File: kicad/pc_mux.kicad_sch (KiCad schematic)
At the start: 12 parts, among them U10 ATF22V10C-7PX, U3 ATF22V10C-10PU, U4 ATF22V10C-10PU, U7 ATF22V10C-7PX, U8 ATF22V10C-7PX, U9 ATF22V10C-7PX

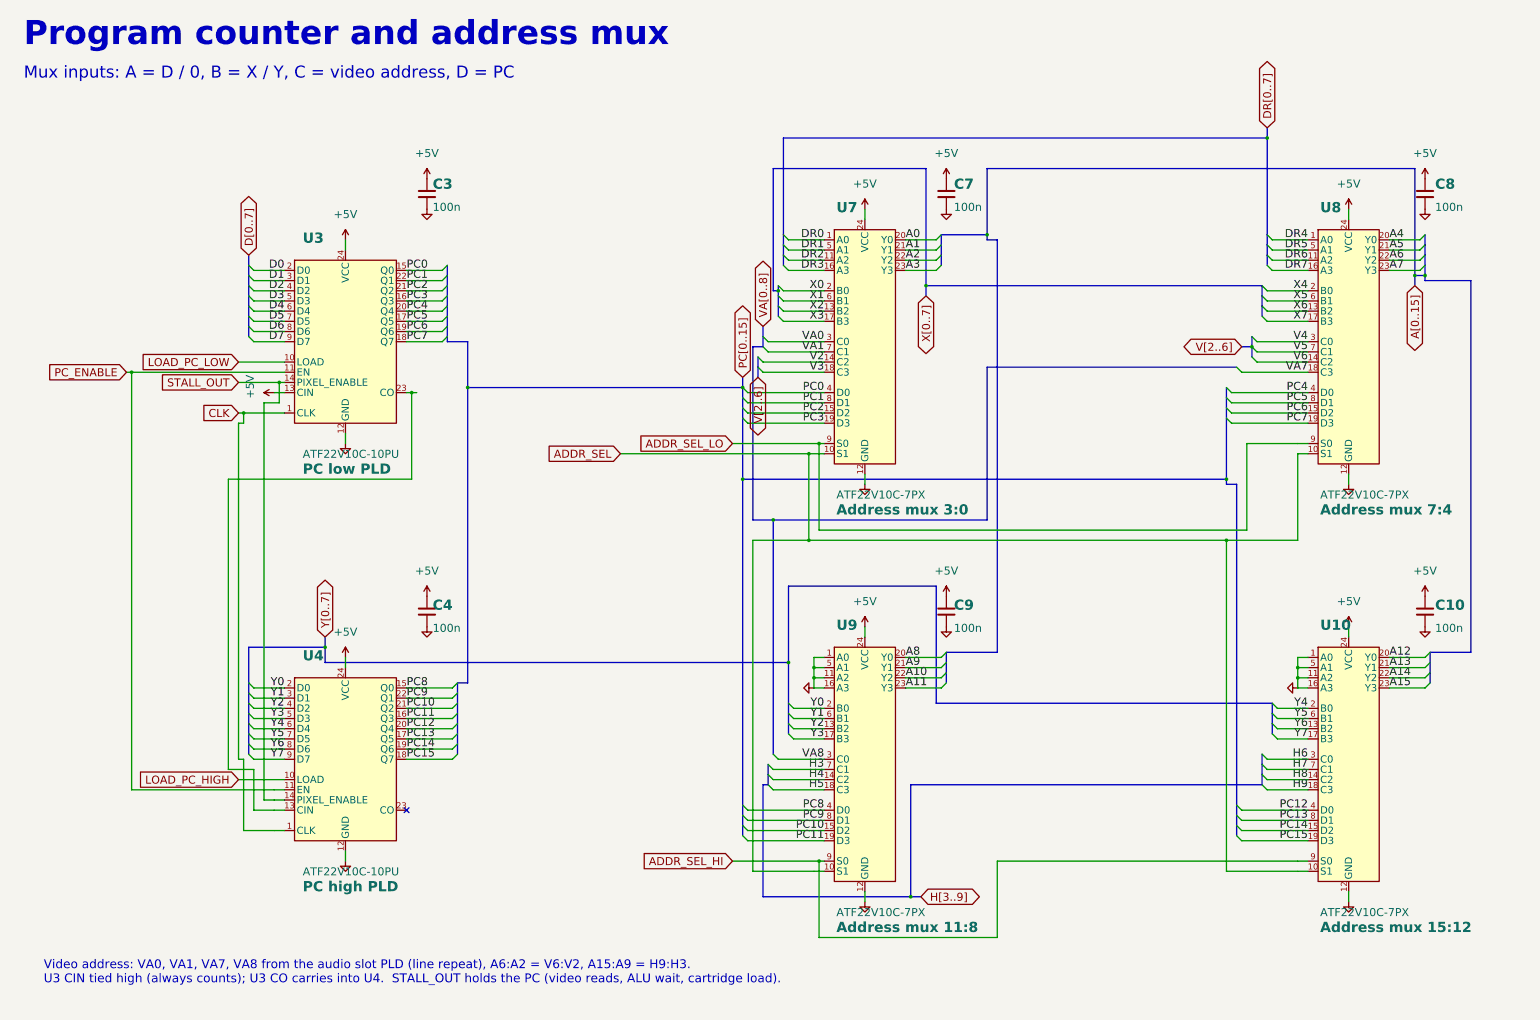
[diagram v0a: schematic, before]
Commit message: Tidy every schematic sheet: spread parts, straight runs, buses kept, horizontal tabs
Shared port, expansion and cartridge sheets laid out by hand; buses from
other sheets get a bus label at each chip, busy control nets a label at
each pin; some PLD and connector symbols reordered so wires run straight;
sideways power symbols read across. 0 netlist problems, no overlaps.

Co-Authored-By: Claude Opus 5.5 (1M context) <noreply@anthropic.com>
Claude-Session: https://claude.ai/code/session_01L9AkLuEg13EebxDmgXsaEp
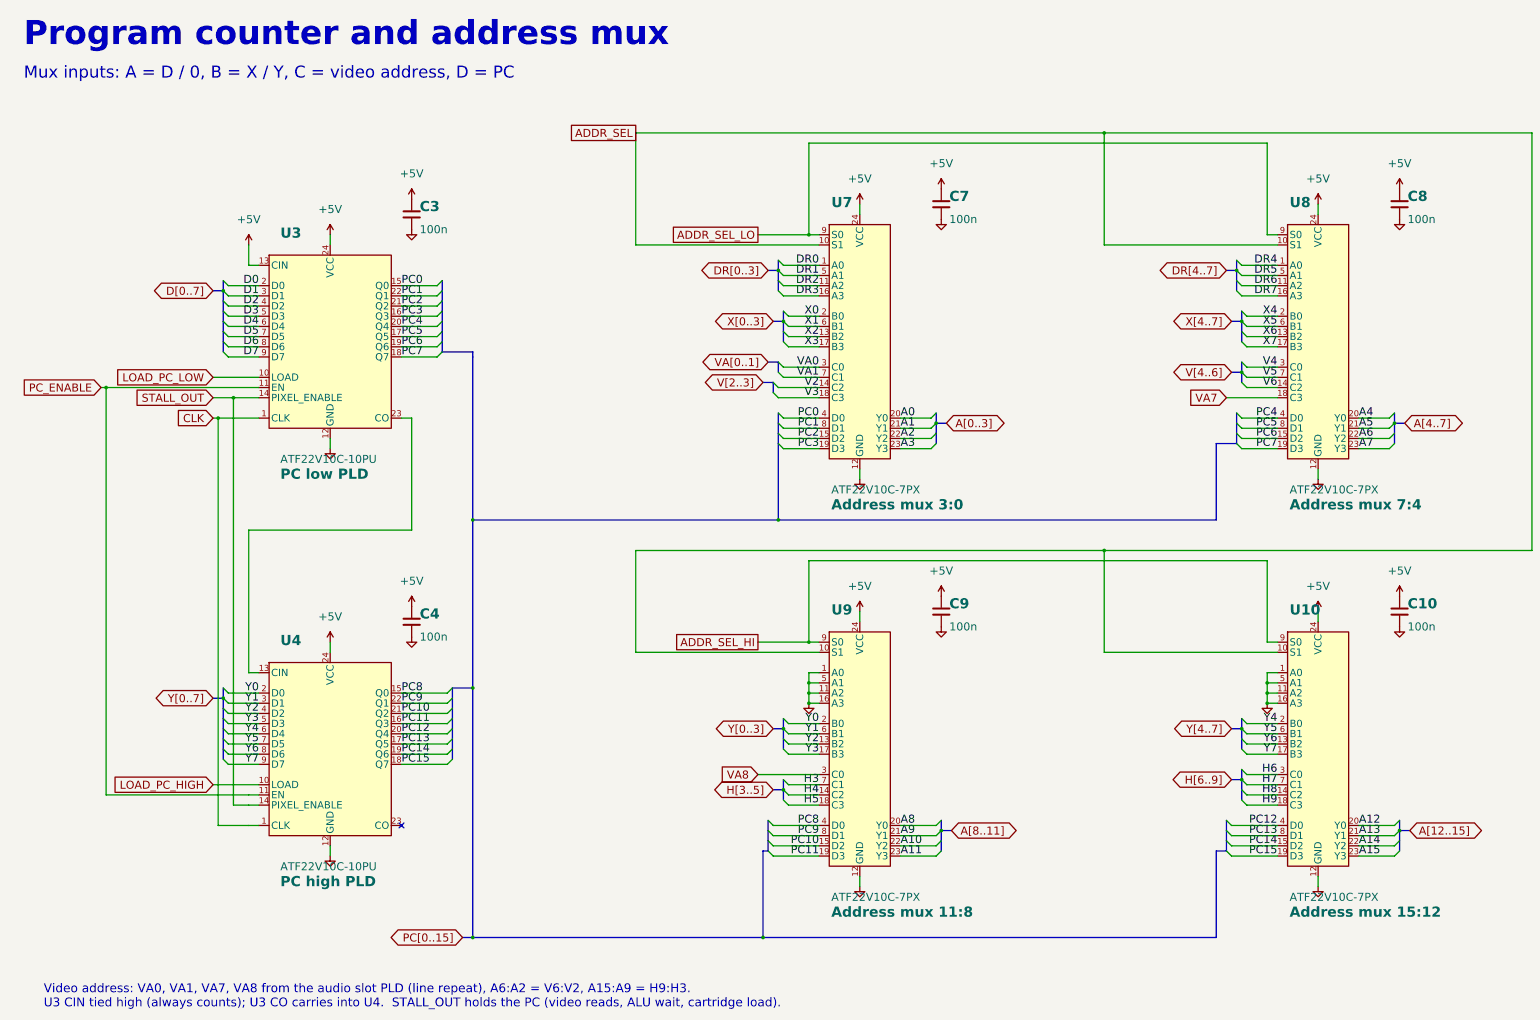
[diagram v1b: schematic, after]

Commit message: Bill of materials for the main board, cartridge and keyboard
Manufacturer and MPN fields on every schematic part (empty where none is
chosen), set from an MPN table in gen_kicad_schematic.py; net tie, cartridge
edge fingers and solder jumper excluded from the BOM.  gen_bom.py groups the
parts by part number into docs/BOM.md and docs/BOM.csv, adding sockets,
shunts, keyboard LEDs, keycaps, stabilizers and the keyboard ribbon cable.

Co-Authored-By: Claude Opus 5.5 (1M context) <noreply@anthropic.com>
Claude-Session: https://claude.ai/code/session_018iEnPngycbxX6Tt4Wzp3zN
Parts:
- U10, U7, U8, U9: MPN (none) -> ATF22V10C-7PX; Manufacturer (none) -> Microchip
- U3, U4: MPN (none) -> ATF22V10C-10PU; Manufacturer (none) -> Microchip

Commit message: Part numbers for the remaining parts; J6 Tensility 54-00174; optional J1 and J9-J12
Every schematic part gets Manufacturer/MPN: Yageo MFR-25 resistors by value,
Bourns 4609X networks, KEMET/TDK ceramics, Panasonic FR electrolytics, ECS
oscillator, Assmann VGA, Sullins headers, Wurth box header, Cherry switches.
Sockets get On Shore numbers (0.3" 24/28-pin are ED241DT/ED281DT; ED28DT is
0.6"). J6 becomes the Tensility 54-00174 TRRS jack with a footprint drawn
from its datasheet. Digi-Key prices from Justin for the oscillator, VGA and
audio jack. The expansion slot sockets and the keyboard header are optional,
with a BOM total without them.

Co-Authored-By: Claude Opus 5.5 (1M context) <noreply@anthropic.com>
Claude-Session: https://claude.ai/code/session_01L9AkLuEg13EebxDmgXsaEp
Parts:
- C10, C3, C4, C7, C8, C9: MPN (none) -> C320C104K5R5TA; Manufacturer (none) -> KEMET

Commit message: Every PLD is an ATF22V10C-7PX (one part number)
Justin: switch the seven main-board -10PU PLDs (Branch, PC x2, H, V,
color decoder, audio slot) and the cartridge loader to the -7PX, for one
part number to buy, program and kit (.52 more per main board). Symbols,
schematics, PDFs, BOM, docs and PLD comments updated; CHIPS.md keeps the
grade each PLD could use.

Co-Authored-By: Claude Opus 5.5 (1M context) <noreply@anthropic.com>
Claude-Session: https://claude.ai/code/session_01JnVuvUvdWezUUU6Sgmg16H
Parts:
- U3, U4: value ATF22V10C-10PU -> ATF22V10C-7PX; MPN ATF22V10C-10PU -> ATF22V10C-7PX
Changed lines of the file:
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@@
   (wire (pts (xy 91.44 119.38) (xy 91.44 121.92)) (stroke (width 0) (type default)))
   (symbol (lib_id "power:GND") (at 91.44 121.92 0) (unit 1) (in_bom yes) (on_board yes) (dnp no) (property "Reference" "#PWR0402" (at 91.44 121.92 0) (effects (font (size 1.27 1.27)) hide)) (property "Value" "GND" (at 91.44 128.27 0) (effects (font (size 2 2)) hide)) (property "Footprint" "" (at 91.44 121.92 0) (effects (font (size 1.27 1.27)) hide)) (property "Datasheet" "" (at 91.44 121.92 0) (effects (font (size 1.27 1.27)) hide)) (pin "1") (instances (project "placard" (path "/e3450542-4ffc-59d4-a4a7-45636233928a/cfc9d041-a0ad-5edc-9a97-521f7f69130f" (reference "#PWR0402") (unit 1)))))
-  (symbol (lib_id "placard:ATF22V10C_PC_COUNTER8") (at 91.44 93.98 0) (unit 1) (in_bom yes) (on_board yes) (dnp no) (property "Reference" "U3" (at 78.994 69.62 0) (effects (font (size 2.54 2.54) bold) (justify left bottom))) (property "Value" "ATF22V10C-10PU" (at 78.994 123.38 0) (effects (font (size 2 2)) (justify left top))) (property "Function" "PC low PLD" (at 78.994 126.78 0) (effects (font (size 2.54 2.54) bold) (justify left top))) (property "Footprint" "Package_DIP:DIP-24_W7.62mm" (at 91.44 93.98 0) (effects (font (size 1.27 1.27)) hide)) (property "Datasheet" "https://ww1.microchip.com/downloads/en/DeviceDoc/doc0735.pdf" (at 91.44 93.98 0) (effects (font (size 1.27 1.27)) hide)) (property "Manufacturer" "Microchip" (at 91.44 93.98 0) (effects (font (size 1.27 1.27)) hide)) (property "MPN" "ATF22V10C-10PU" (at 91.44 93.98 0) (effects (font (size 1.27 1.27)) hide)) (property "PLD" "ATF22V10_PC_COUNTER8.pld" (at 91.44 93.98 0) (effects (font (size 1.27 1.27)) hide)) (pin "13") (pin "2") (pin "3") (pin "4") (pin "5") (pin "6") (pin "7") (pin "8") (pin "9") (pin "10") (pin "11") (pin "14") (pin "1") (pin "15") (pin "22") (pin "21") (pin "16") (pin "20") (pin "17") (pin "19") (pin "18") (pin "23") (pin "24") (pin "12") (instances (project "placard" (path "/e3450542-4ffc-59d4-a4a7-45636233928a/cfc9d041-a0ad-5edc-9a97-521f7f69130f" (reference "U3") (unit 1)))))
+  (symbol (lib_id "placard:ATF22V10C_PC_COUNTER8") (at 91.44 93.98 0) (unit 1) (in_bom yes) (on_board yes) (dnp no) (property "Reference" "U3" (at 78.994 69.62 0) (effects (font (size 2.54 2.54) bold) (justify left bottom))) (property "Value" "ATF22V10C-7PX" (at 78.994 123.38 0) (effects (font (size 2 2)) (justify left top))) (property "Function" "PC low PLD" (at 78.994 126.78 0) (effects (font (size 2.54 2.54) bold) (justify left top))) (property "Footprint" "Package_DIP:DIP-24_W7.62mm" (at 91.44 93.98 0) (effects (font (size 1.27 1.27)) hide)) (property "Datasheet" "https://ww1.microchip.com/downloads/en/DeviceDoc/doc0735.pdf" (at 91.44 93.98 0) (effects (font (size 1.27 1.27)) hide)) (property "Manufacturer" "Microchip" (at 91.44 93.98 0) (effects (font (size 1.27 1.27)) hide)) (property "MPN" "ATF22V10C-7PX" (at 91.44 93.98 0) (effects (font (size 1.27 1.27)) hide)) (property "PLD" "ATF22V10_PC_COUNTER8.pld" (at 91.44 93.98 0) (effects (font (size 1.27 1.27)) hide)) (pin "13") (pin "2") (pin "3") (pin "4") (pin "5") (pin "6") (pin "7") (pin "8") (pin "9") (pin "10") (pin "11") (pin "14") (pin "1") (pin "15") (pin "22") (pin "21") (pin "16") (pin "20") (pin "17") (pin "19") (pin "18") (pin "23") (pin "24") (pin "12") (instances (project "placard" (path "/e3450542-4ffc-59d4-a4a7-45636233928a/cfc9d041-a0ad-5edc-9a97-521f7f69130f" (reference "U3") (unit 1)))))
   (symbol (lib_id "power:+5V") (at 111.76 59.69 0) (unit 1) (in_bom yes) (on_board yes) (dnp no) (property "Reference" "#PWR0403" (at 111.76 59.69 0) (effects (font (size 1.27 1.27)) hide)) (property "Value" "+5V" (at 111.76 53.34 0) (effects (font (size 2 2)))) (property "Footprint" "" (at 111.76 59.69 0) (effects (font (size 1.27 1.27)) hide)) (property "Datasheet" "" (at 111.76 59.69 0) (effects (font (size 1.27 1.27)) hide)) (pin "1") (instances (project "placard" (path "/e3450542-4ffc-59d4-a4a7-45636233928a/cfc9d041-a0ad-5edc-9a97-521f7f69130f" (reference "#PWR0403") (unit 1)))))
   (symbol (lib_id "power:GND") (at 111.76 67.31 0) (unit 1) (in_bom yes) (on_board yes) (dnp no) (property "Reference" "#PWR0404" (at 111.76 67.31 0) (effects (font (size 1.27 1.27)) hide)) (property "Value" "GND" (at 111.76 73.66 0) (effects (font (size 2 2)) hide)) (property "Footprint" "" (at 111.76 67.31 0) (effects (font (size 1.27 1.27)) hide)) (property "Datasheet" "" (at 111.76 67.31 0) (effects (font (size 1.27 1.27)) hide)) (pin "1") (instances (project "placard" (path "/e3450542-4ffc-59d4-a4a7-45636233928a/cfc9d041-a0ad-5edc-9a97-521f7f69130f" (reference "#PWR0404") (unit 1)))))
@@
   (wire (pts (xy 91.44 220.98) (xy 91.44 223.52)) (stroke (width 0) (type default)))
   (symbol (lib_id "power:GND") (at 91.44 223.52 0) (unit 1) (in_bom yes) (on_board yes) (dnp no) (property "Reference" "#PWR0406" (at 91.44 223.52 0) (effects (font (size 1.27 1.27)) hide)) (property "Value" "GND" (at 91.44 229.87 0) (effects (font (size 2 2)) hide)) (property "Footprint" "" (at 91.44 223.52 0) (effects (font (size 1.27 1.27)) hide)) (property "Datasheet" "" (at 91.44 223.52 0) (effects (font (size 1.27 1.27)) hide)) (pin "1") (instances (project "placard" (path "/e3450542-4ffc-59d4-a4a7-45636233928a/cfc9d041-a0ad-5edc-9a97-521f7f69130f" (reference "#PWR0406") (unit 1)))))
-  (symbol (lib_id "placard:ATF22V10C_PC_COUNTER8") (at 91.44 195.58 0) (unit 1) (in_bom yes) (on_board yes) (dnp no) (property "Reference" "U4" (at 78.994 171.22 0) (effects (font (size 2.54 2.54) bold) (justify left bottom))) (property "Value" "ATF22V10C-10PU" (at 78.994 224.98 0) (effects (font (size 2 2)) (justify left top))) (property "Function" "PC high PLD" (at 78.994 228.38 0) (effects (font (size 2.54 2.54) bold) (justify left top))) (property "Footprint" "Package_DIP:DIP-24_W7.62mm" (at 91.44 195.58 0) (effects (font (size 1.27 1.27)) hide)) (property "Datasheet" "https://ww1.microchip.com/downloads/en/DeviceDoc/doc0735.pdf" (at 91.44 195.58 0) (effects (font (size 1.27 1.27)) hide)) (property "Manufacturer" "Microchip" (at 91.44 195.58 0) (effects (font (size 1.27 1.27)) hide)) (property "MPN" "ATF22V10C-10PU" (at 91.44 195.58 0) (effects (font (size 1.27 1.27)) hide)) (property "PLD" "ATF22V10_PC_COUNTER8.pld" (at 91.44 195.58 0) (effects (font (size 1.27 1.27)) hide)) (pin "13") (pin "2") (pin "3") (pin "4") (pin "5") (pin "6") (pin "7") (pin "8") (pin "9") (pin "10") (pin "11") (pin "14") (pin "1") (pin "15") (pin "22") (pin "21") (pin "16") (pin "20") (pin "17") (pin "19") (pin "18") (pin "23") (pin "24") (pin "12") (instances (project "placard" (path "/e3450542-4ffc-59d4-a4a7-45636233928a/cfc9d041-a0ad-5edc-9a97-521f7f69130f" (reference "U4") (unit 1)))))
+  (symbol (lib_id "placard:ATF22V10C_PC_COUNTER8") (at 91.44 195.58 0) (unit 1) (in_bom yes) (on_board yes) (dnp no) (property "Reference" "U4" (at 78.994 171.22 0) (effects (font (size 2.54 2.54) bold) (justify left bottom))) (property "Value" "ATF22V10C-7PX" (at 78.994 224.98 0) (effects (font (size 2 2)) (justify left top))) (property "Function" "PC high PLD" (at 78.994 228.38 0) (effects (font (size 2.54 2.54) bold) (justify left top))) (property "Footprint" "Package_DIP:DIP-24_W7.62mm" (at 91.44 195.58 0) (effects (font (size 1.27 1.27)) hide)) (property "Datasheet" "https://ww1.microchip.com/downloads/en/DeviceDoc/doc0735.pdf" (at 91.44 195.58 0) (effects (font (size 1.27 1.27)) hide)) (property "Manufacturer" "Microchip" (at 91.44 195.58 0) (effects (font (size 1.27 1.27)) hide)) (property "MPN" "ATF22V10C-7PX" (at 91.44 195.58 0) (effects (font (size 1.27 1.27)) hide)) (property "PLD" "ATF22V10_PC_COUNTER8.pld" (at 91.44 195.58 0) (effects (font (size 1.27 1.27)) hide)) (pin "13") (pin "2") (pin "3") (pin "4") (pin "5") (pin "6") (pin "7") (pin "8") (pin "9") (pin "10") (pin "11") (pin "14") (pin "1") (pin "15") (pin "22") (pin "21") (pin "16") (pin "20") (pin "17") (pin "19") (pin "18") (pin "23") (pin "24") (pin "12") (instances (project "placard" (path "/e3450542-4ffc-59d4-a4a7-45636233928a/cfc9d041-a0ad-5edc-9a97-521f7f69130f" (reference "U4") (unit 1)))))
   (symbol (lib_id "power:+5V") (at 111.76 161.29 0) (unit 1) (in_bom yes) (on_board yes) (dnp no) (property "Reference" "#PWR0407" (at 111.76 161.29 0) (effects (font (size 1.27 1.27)) hide)) (property "Value" "+5V" (at 111.76 154.94 0) (effects (font (size 2 2)))) (property "Footprint" "" (at 111.76 161.29 0) (effects (font (size 1.27 1.27)) hide)) (property "Datasheet" "" (at 111.76 161.29 0) (effects (font (size 1.27 1.27)) hide)) (pin "1") (instances (project "placard" (path "/e3450542-4ffc-59d4-a4a7-45636233928a/cfc9d041-a0ad-5edc-9a97-521f7f69130f" (reference "#PWR0407") (unit 1)))))
   (symbol (lib_id "power:GND") (at 111.76 168.91 0) (unit 1) (in_bom yes) (on_board yes) (dnp no) (property "Reference" "#PWR0408" (at 111.76 168.91 0) (effects (font (size 1.27 1.27)) hide)) (property "Value" "GND" (at 111.76 175.26 0) (effects (font (size 2 2)) hide)) (property "Footprint" "" (at 111.76 168.91 0) (effects (font (size 1.27 1.27)) hide)) (property "Datasheet" "" (at 111.76 168.91 0) (effects (font (size 1.27 1.27)) hide)) (pin "1") (instances (project "placard" (path "/e3450542-4ffc-59d4-a4a7-45636233928a/cfc9d041-a0ad-5edc-9a97-521f7f69130f" (reference "#PWR0408") (unit 1)))))

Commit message: Kit footprints: DIP sockets with puller room and part number, resistors with value
Justin: put the chip-puller room in the socket footprints (User.Eco1,
2.5 mm past each end) and the part number in silkscreen between the pin
rows; resistors get their value in silkscreen on the body. New
gen_kicad_kit_footprints.py derives them from KiCad's stock footprints;
schematic, symbols, BOM and PDFs now name them. The board file is left
as is (Justin is editing it): Update PCB from Schematic swaps them in.

Co-Authored-By: Claude Opus 5.5 (1M context) <noreply@anthropic.com>
Claude-Session: https://claude.ai/code/session_01JnVuvUvdWezUUU6Sgmg16H
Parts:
- U10, U3, U4, U7, U8, U9: footprint Package_DIP:DIP-24_W7.62mm -> placard:DIP-24_W7.62mm_Socket_Puller
